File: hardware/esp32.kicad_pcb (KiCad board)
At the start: 4 copper layers, 60 x 40 mm, 86 parts, among them J101 USB-C-2, P101 PWR, P201 CON-SENSOR2, P202 CON-SENSOR2, P203 CON-SENSOR2, P204 CON-SENSOR2, P205 CON-SENSOR2, P206 CON-SENSOR2, Q101 NPN, Q102 NPN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

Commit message: specify diodes
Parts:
- D103, D104: value TBD -> BAT54HT1G
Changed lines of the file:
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@@
-(kicad_pcb (version 20171130) (host pcbnew 5.1.5-52549c5~84~ubuntu18.04.1)
+(kicad_pcb (version 20171130) (host pcbnew 5.1.5-52549c5~86~ubuntu18.04.1)
   (general
     (thickness 1.6)
@@
       (effects (font (size 0.29972 0.29972) (thickness 0.07493)))
     )
-    (fp_text value TBD (at 0.04 0.05) (layer F.Fab)
+    (fp_text value BAT54HT1G (at 0.04 0.05) (layer F.Fab)
       (effects (font (size 0.29972 0.29972) (thickness 0.07493)))
     )
@@
       (effects (font (size 0.29972 0.29972) (thickness 0.07493)))
     )
-    (fp_text value TBD (at 0.04 0.05) (layer F.Fab)
+    (fp_text value BAT54HT1G (at 0.04 0.05) (layer F.Fab)
       (effects (font (size 0.29972 0.29972) (thickness 0.07493)))
     )

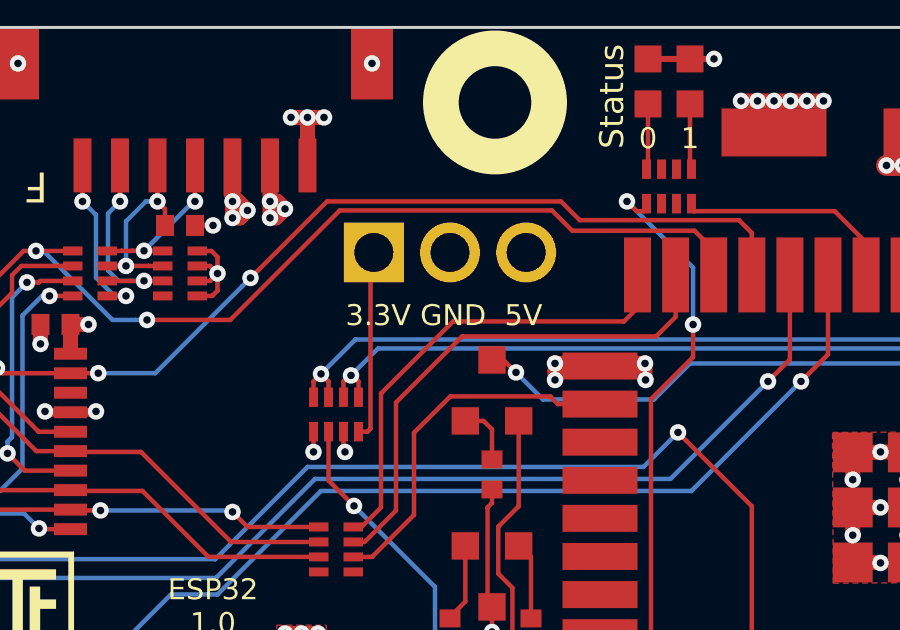
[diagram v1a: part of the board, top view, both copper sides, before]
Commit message: fix header silkscreen
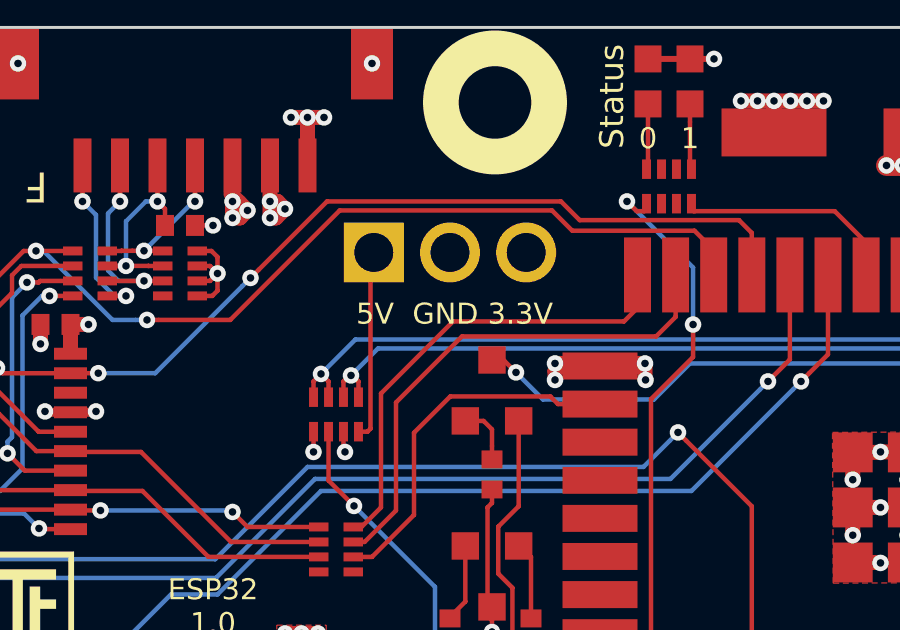
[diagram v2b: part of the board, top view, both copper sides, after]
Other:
- board text added: "5V GND 3.3V"
- board text removed: "3.3V GND 5V"
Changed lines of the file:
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@@
     (effects (font (size 0.8 0.8) (thickness 0.15)))
   )
-  (gr_text "3.3V GND  5V" (at 149.6 133.25) (layer F.SilkS)
+  (gr_text " 5V  GND 3.3V" (at 149.8 133.2) (layer F.SilkS)
     (effects (font (size 0.7 0.7) (thickness 0.15)))
   )

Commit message: define parts
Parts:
- C112: value TBD -> DNP
- R104: value 22.1k -> 22k
- R105: value 47.5k -> 47k

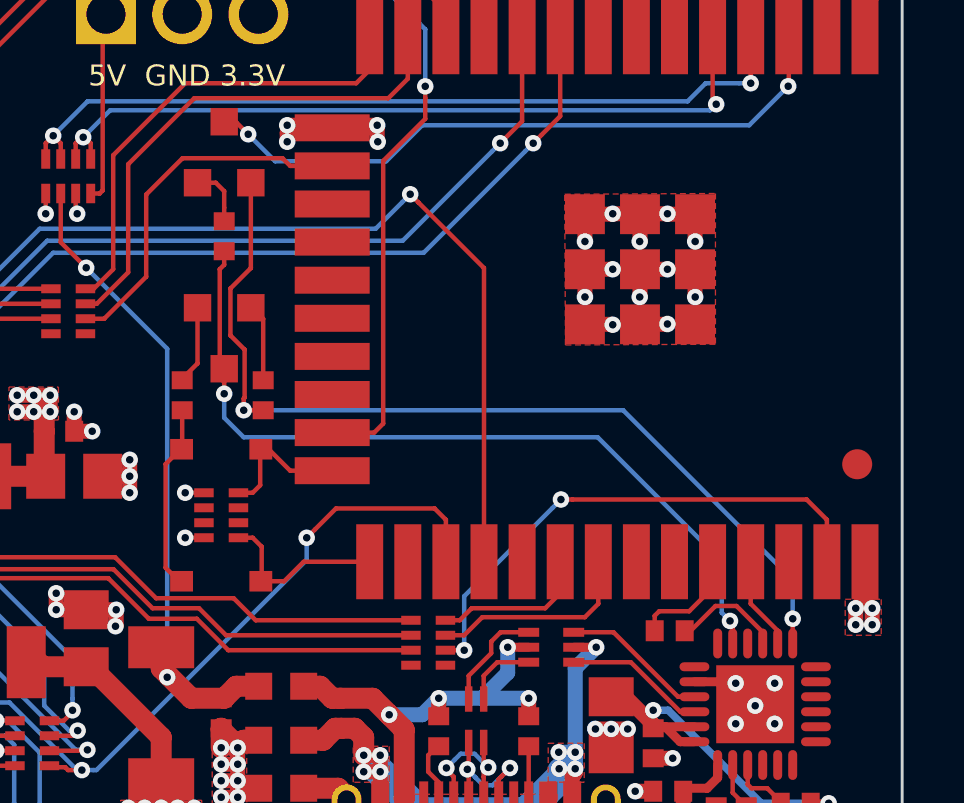
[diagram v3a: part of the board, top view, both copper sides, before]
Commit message: bugfix flash circuitry
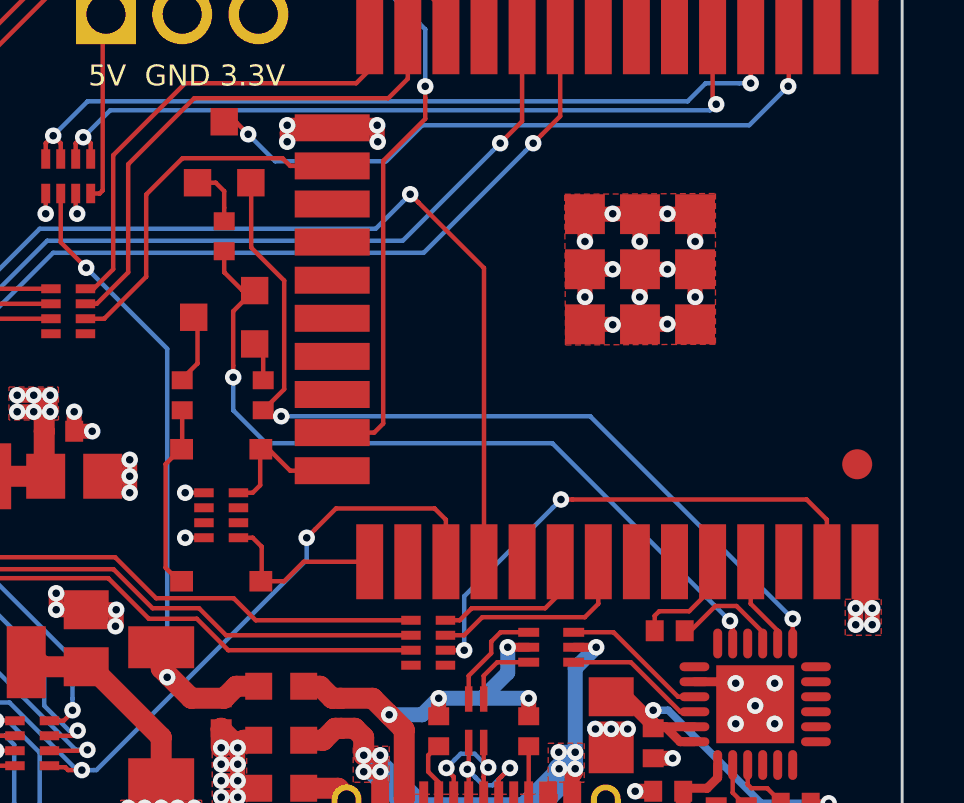
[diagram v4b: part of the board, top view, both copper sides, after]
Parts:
- R107: value 470 -> 100
- moved Q102 0.70 mm to (151.2, 141.2), turned to 270 degrees
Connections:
- R108 pad 1: Net-(Q102-PadC) -> Net-(Q102-PadE)
- R110 pad 1: Net-(Q102-PadE) -> Net-(Q102-PadC)
- U103 pad 23: Net-(Q102-PadC) -> Net-(Q102-PadE)
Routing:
- net Net-(Q102-PadC): track 27.1 -> 2.65 mm, vias 2 -> 0
- net Net-(Q102-PadE): track 2.65 -> 26.5 mm, vias 0 -> 2
- net Net-(Q101-PadE): track 31.5 -> 29.7 mm
- net Net-(Q102-PadB): track 2.62 -> 1.32 mm

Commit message: fix esp32
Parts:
- Q101, Q102: value NPN -> BC817
- U104: value ESP32-WROOM-32 -> ESP32WRM32E128PH

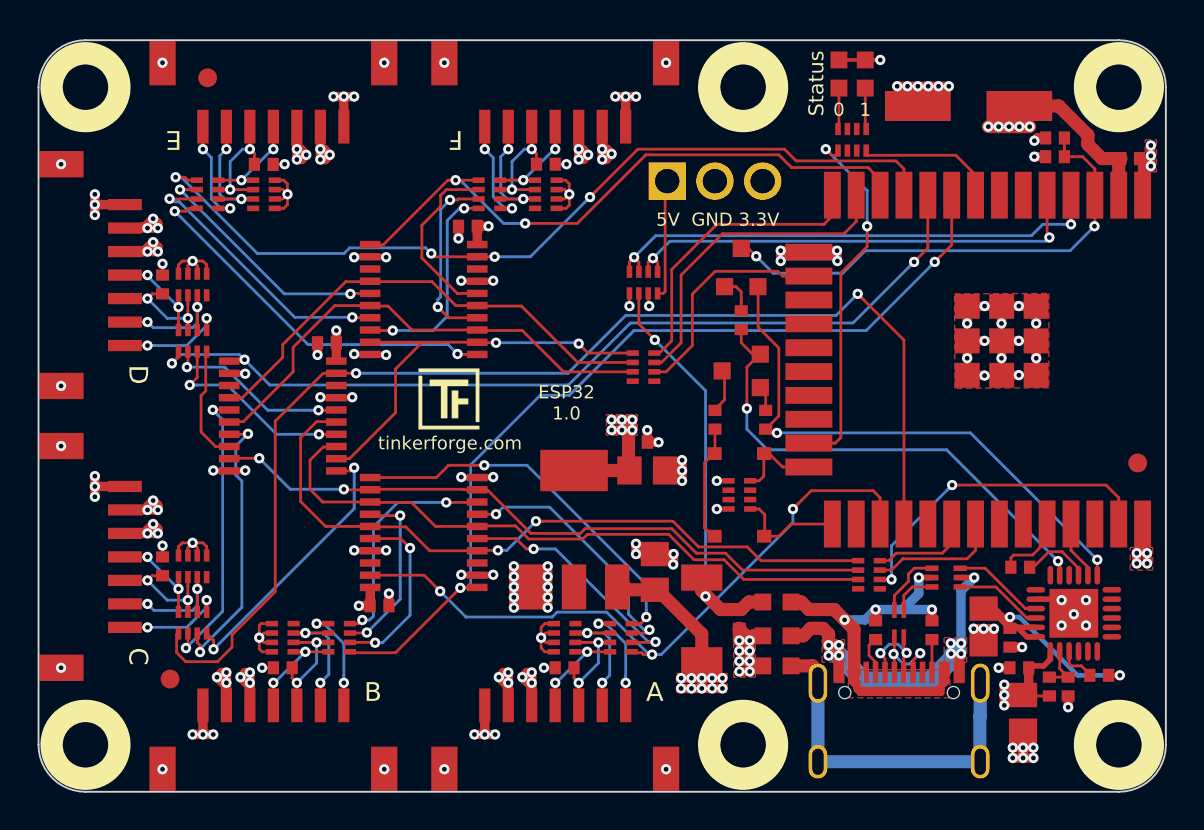
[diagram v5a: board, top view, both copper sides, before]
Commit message: esp brick version 1.1
changed power input connector 2 pole
fix npn cricuitry
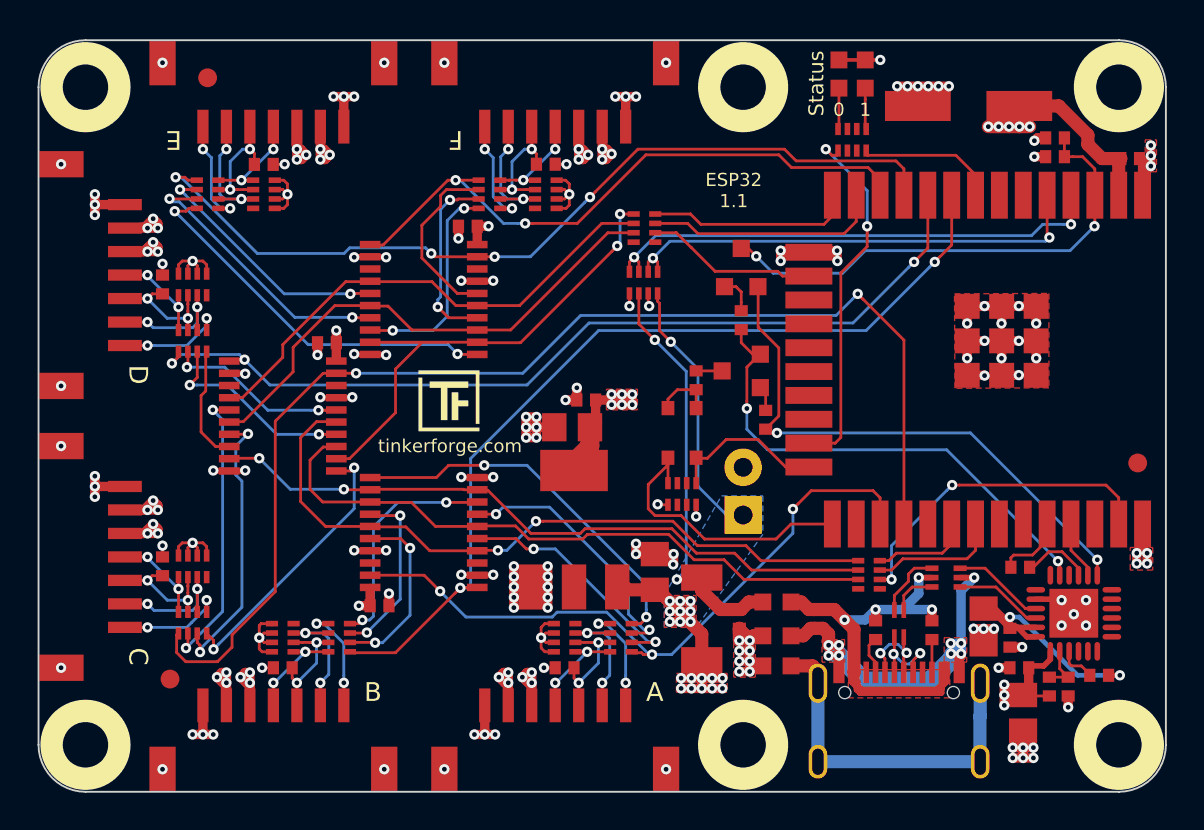
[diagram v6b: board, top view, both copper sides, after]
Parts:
- P101: footprint kicad-libraries:PIN_ARRAY_3X1 -> kicad-libraries:PIN_ARRAY_2X1
- moved P101 16.6 mm to (151.3, 147.7), turned to 90 degrees
- moved RP101 7.40 mm to (146.1, 133.7)
- moved VAL 7.00 mm to (146.8, 143.7)
- moved D103 6.69 mm to (147.3, 144.6), turned to 90 degrees
- moved C108 4.61 mm to (142.2, 144.2), turned to 0 degrees
- moved C109 3.55 mm to (142.9, 142.8), turned to 0 degrees
- moved RP103 3.05 mm to (148.1, 147.8), turned to 0 degrees
- moved D104 2.55 mm to (148.8, 144.6), turned to 90 degrees
- moved R110 2.33 mm to (148.8, 141.8)
- moved VAL 2.00 mm to (135.8, 143.7)
- moved G*** 0.10 mm to (135.7, 142.8)
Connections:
- RP103 pad 1: ESP_IO0 -> 3V3
- RP103 pad 4: ESP_IO2 -> 3V3
- RP103 pad 5: 3V3 -> ESP_IO2
- RP103 pad 8: 3V3 -> ESP_IO0
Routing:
- net ESP_IO0: track 5.87 -> 15.1 mm
- net 5V: track 65.3 -> 72.6 mm, vias 31 -> 41
- net Net-(RP101-Pad8): track 15.8 -> 10.9 mm
- net Net-(RP101-Pad7): track 17.4 -> 12.6 mm
- net ESP_IO2: track 4.73 -> 8.42 mm
- net B0-MISO: track 22.8 -> 26.3 mm
- net Net-(D103-Pad2): track 6.20 -> 3.11 mm
- net Net-(RP101-Pad6): track 12.2 -> 9.13 mm
- net GND: track 127.3 -> 130.1 mm, vias 132 -> 135
- net B0-MOSI: track 26.3 -> 27.6 mm
- net Net-(Q102-PadC): track 2.65 -> 1.40 mm
- net B0-CLK: track 26.3 -> 26.8 mm
- added copper zone on B.Cu, net 5V
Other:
- board text added: "ESP32 1.1"
- board text removed: "5V GND 3.3V"
- board text removed: "ESP32 1.0"

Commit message: add larger header
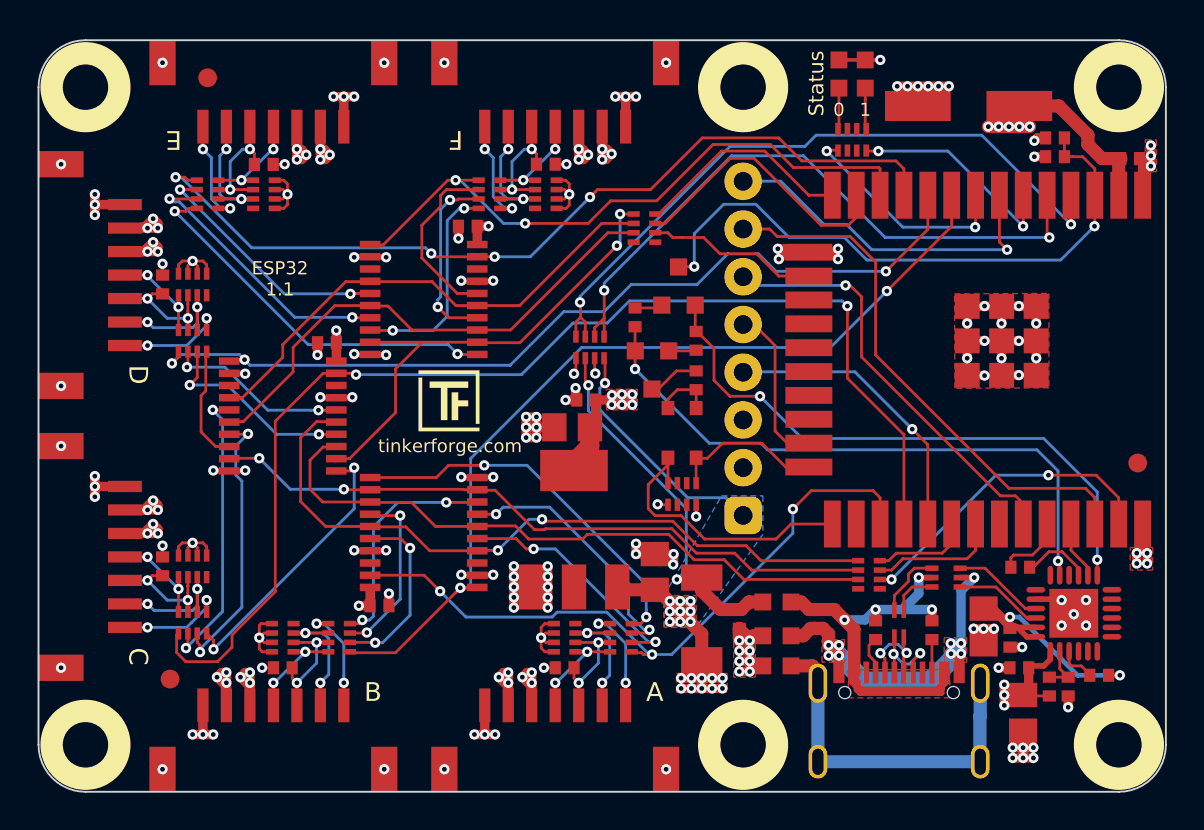
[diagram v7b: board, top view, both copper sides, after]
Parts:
- P101: value PWR -> EXT_HEADER; footprint kicad-libraries:PIN_ARRAY_2X1 -> kicad-libraries:pin_array_1x8-P2mm_D1mm
- moved P101 7.60 mm to (151.3, 140.1)
- moved R108 5.65 mm to (145.6, 138.4)
- moved R109 5.60 mm to (148.8, 139.7), turned to 270 degrees
- moved Q102 4.75 mm to (146.4, 141.2), turned to 0 degrees
- moved RP104 4.47 mm to (143.2, 140.0)
- moved Q101 3.48 mm to (147.9, 136.7)
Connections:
- U104 pad 23: Net-(RP105-Pad5) -> ESP_IO15
- U104 pad 29: Net-(U104-Pad29) -> ESP_IO5
- U104 pad 33: Net-(U104-Pad33) -> ESP_IO21
- U104 pad 36: Net-(U104-Pad36) -> ESP_IO22
- U104 pad 6: Net-(U104-Pad6) -> Net-(RP105-Pad8)
- U104 pad 7: Net-(U104-Pad7) -> ESP_IO35
- U104 pad 8: Net-(RP105-Pad8) -> Net-(RP105-Pad5)
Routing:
- net ESP_IO22: track 0.00 -> 29.6 mm
- net ESP_IO21: track 0.00 -> 22.9 mm, vias 0 -> 1
- net ESP_IO35: track 0.00 -> 18.7 mm, vias 0 -> 1
- net ESP_IO5: track 0.00 -> 15.7 mm, vias 0 -> 1
- net ESP_ADC_5V: track 27.3 -> 36.6 mm
- net ESP_ADC_VUSB: track 25.6 -> 34.7 mm
- net ESP_IO15: track 0.00 -> 8.82 mm
- net Net-(RP105-Pad5): track 19.7 -> 11.9 mm
- net ESP_EN: track 26.3 -> 32.5 mm
- net Net-(Q102-PadE): track 26.5 -> 32.6 mm
- net Net-(RP105-Pad8): track 7.50 -> 11.7 mm, vias 0 -> 2
- net Net-(RP101-Pad7): track 12.6 -> 15.0 mm
- net Net-(C101-Pad2): track 22.6 -> 20.3 mm
- net Net-(Q101-PadE): track 29.7 -> 31.7 mm
- net 5V: track 72.6 -> 71.2 mm
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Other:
- board text added: "Copyright Tinkerforge GmbH 2020. This documentation describes Open Hardware and is licensed under the CERN OHL v. 1.1. You may redistribute and modify this documentation under the terms of the CERN OHL v.1.1. (http://ohwr.org/cernohl). This documentation is distributed WITHOUT ANY EXPRESS OR IMPLIED WARRANTY, INCLUDING OF MERCHANTABILITY, SATISFACTORY QUALITY AND FITNESS FOR A PARTICULAR PURPOSE.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"
- board text added: "IO35 IO22 IO21 IO15 IO5 3V3 GND 5V"
